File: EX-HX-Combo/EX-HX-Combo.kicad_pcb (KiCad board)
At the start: 2 copper layers, 150.2 x 124.5 mm, 41 parts, among them CN1 DB9 Male, J1 IDE_CONNECTOR, J200 Bus_Tandy_Plus_Through, J3 Bus_Tandy_Plus, SW1 SW_DIP_x10, U1 BIOS FLASH, U2 74HCT245, U3 1.8432 MHz, U4 DS1315, U5 AS6C4008-55PCN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

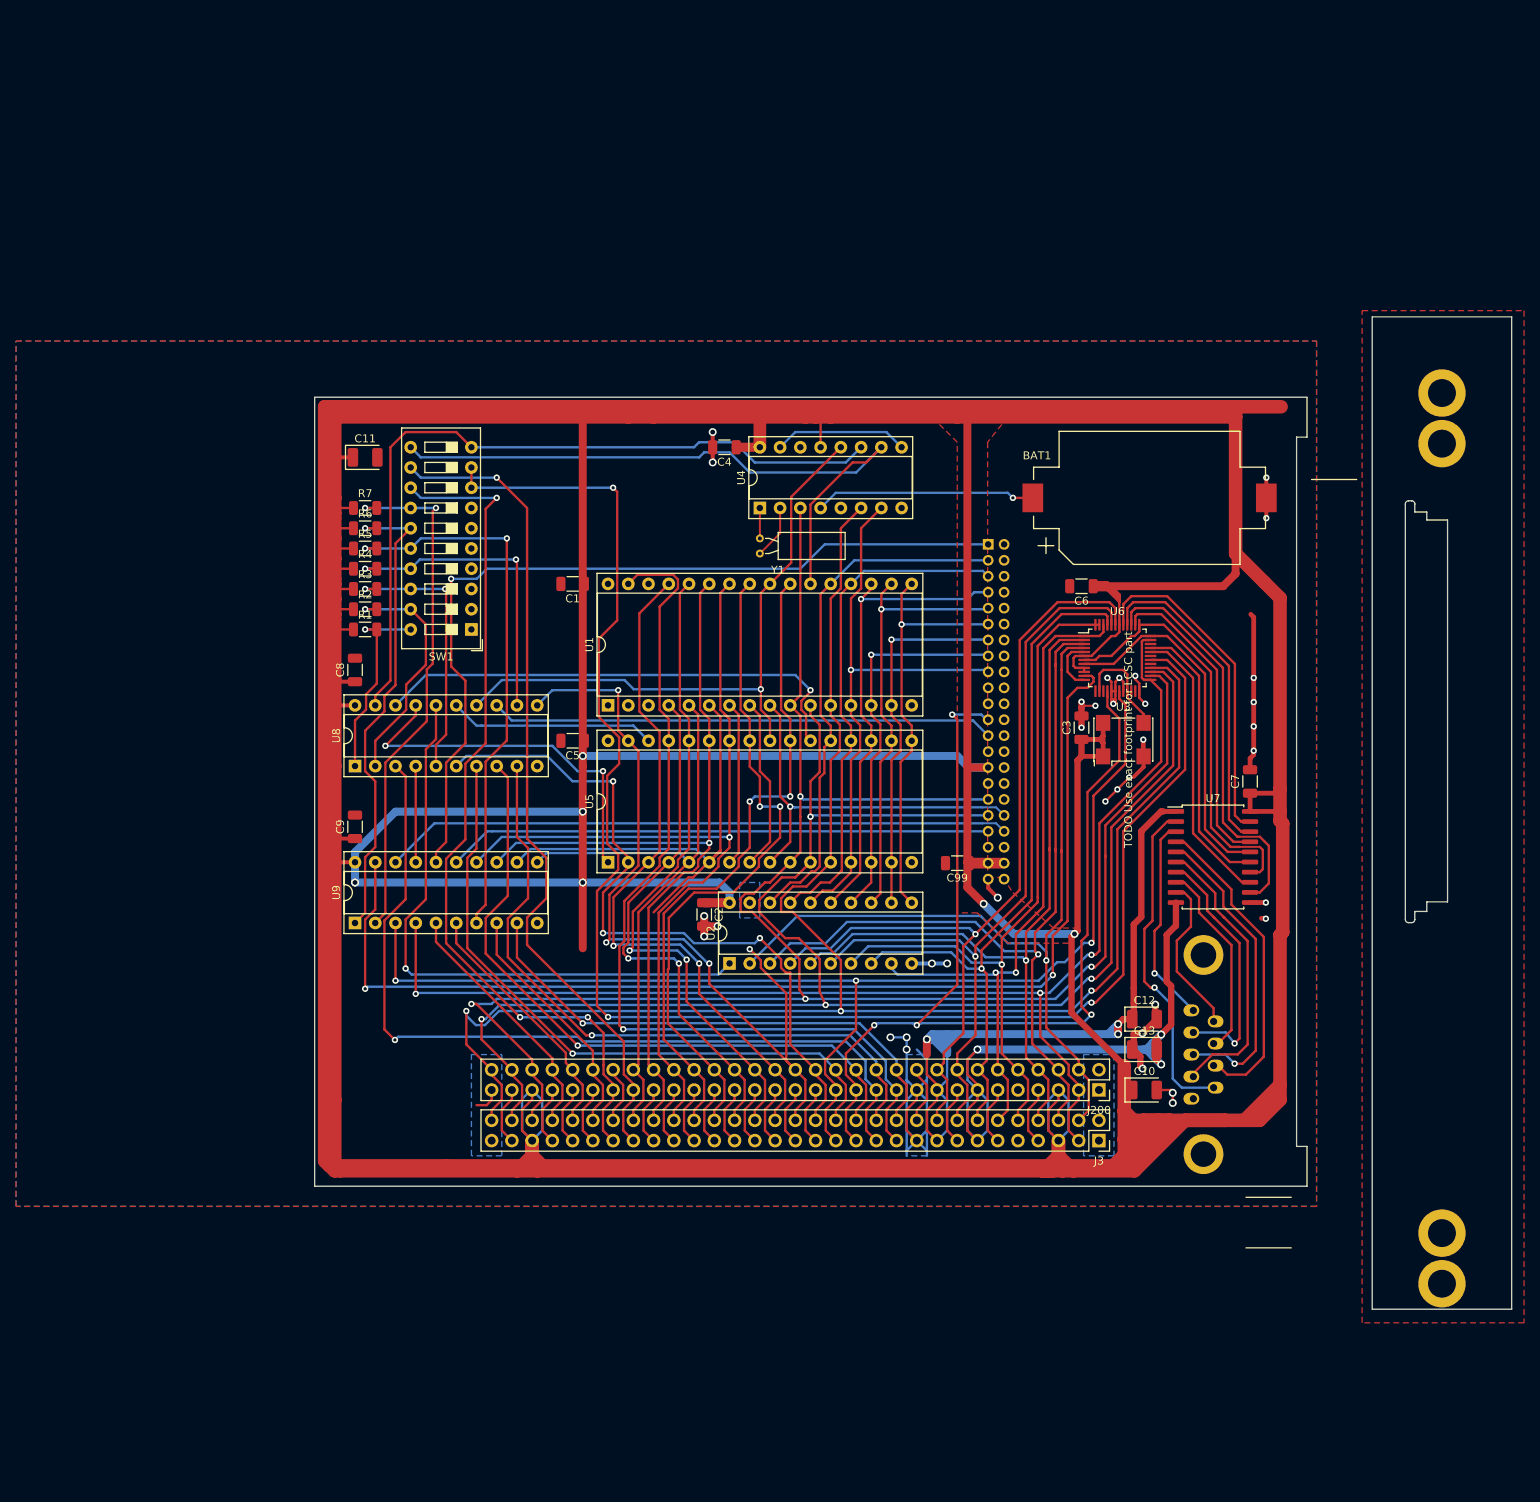
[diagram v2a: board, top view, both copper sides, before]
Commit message: EX-HX-Combo layout work: All connections have been made, in progress on tidy up.
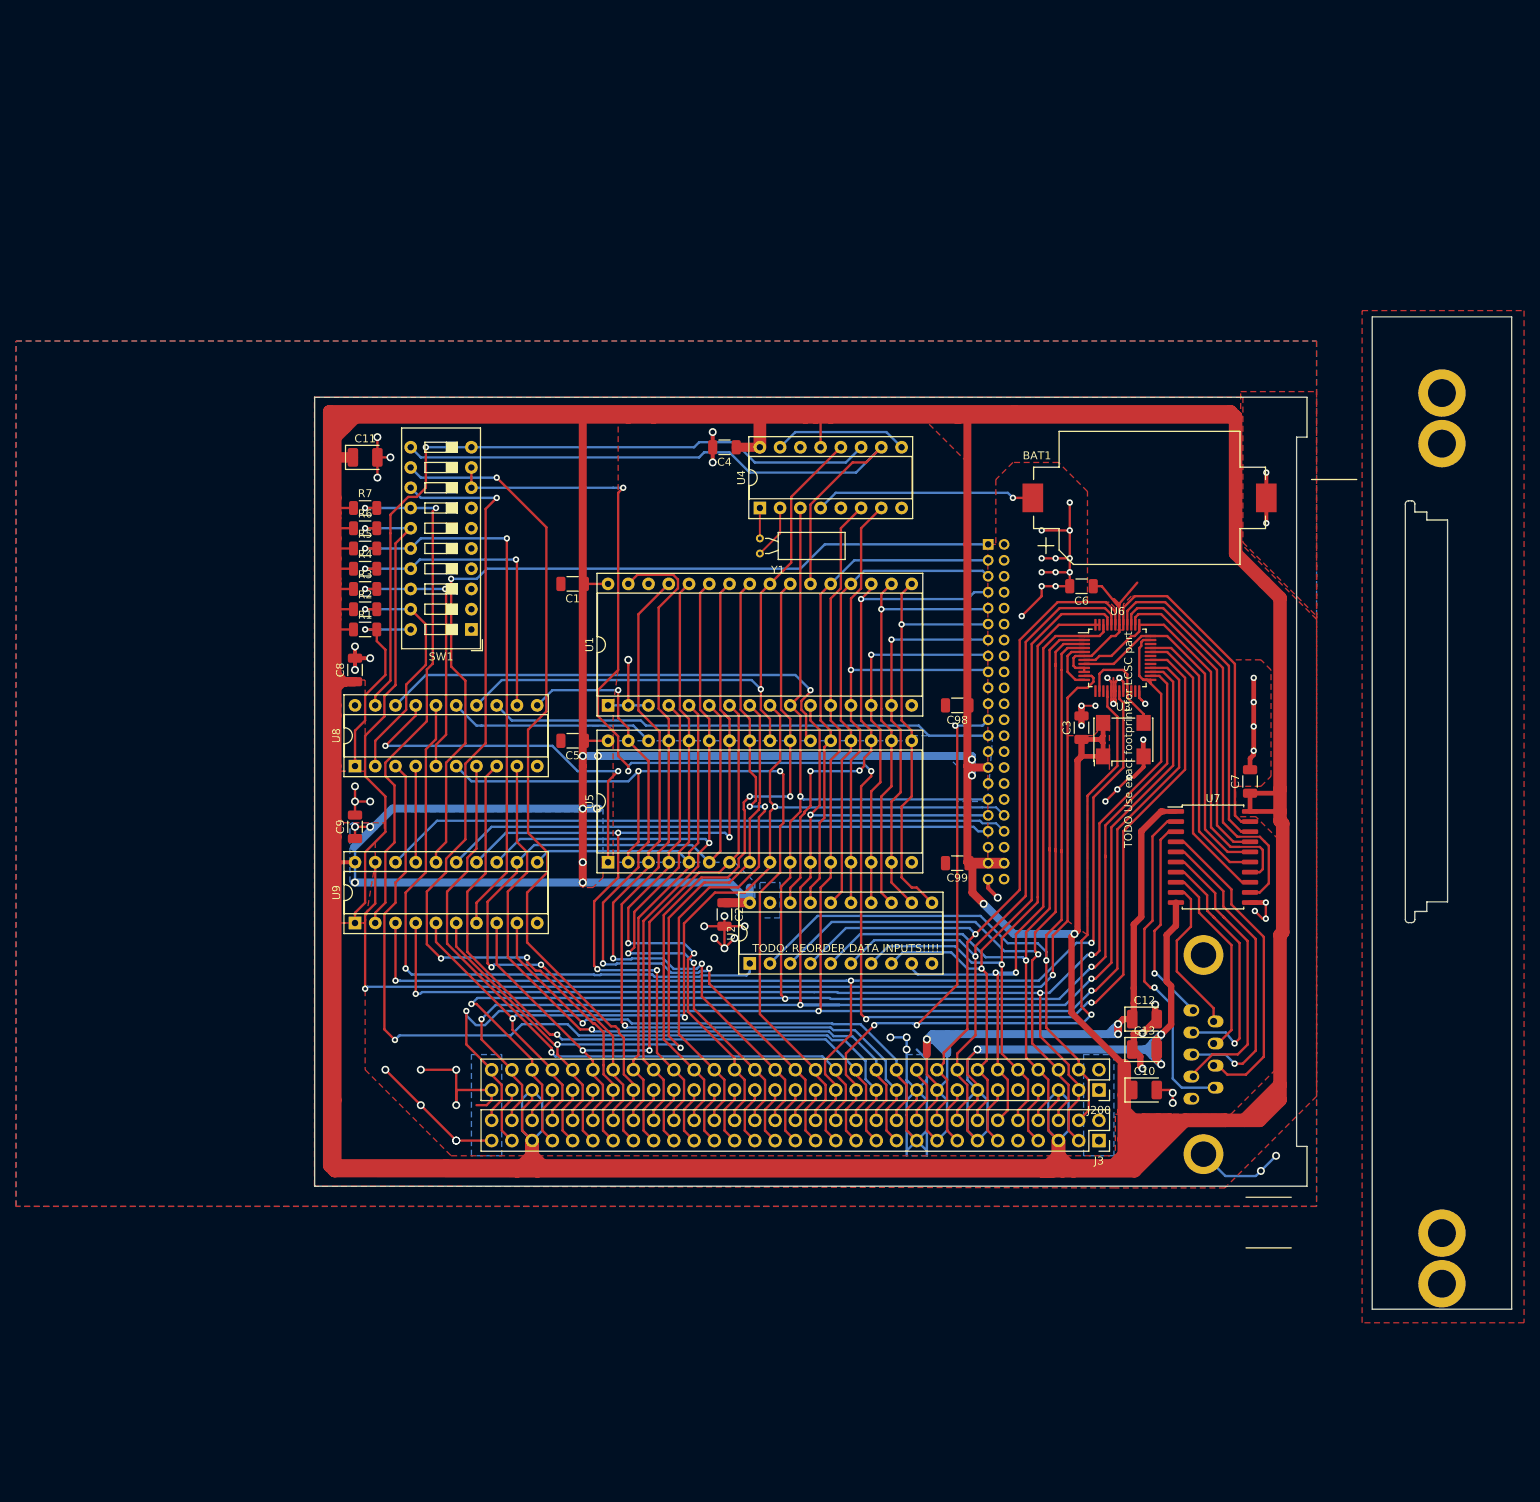
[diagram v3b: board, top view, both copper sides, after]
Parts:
- added C98: 0.1uF, Capacitor_SMD:C_1206_3216Metric, F.Cu at (200.7, 76.2)
- moved C2 2.54 mm to (171.4, 102.4)
- moved U2 2.54 mm to (174.6, 108.6)
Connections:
- U2 pad 15: D5_BUF -> D0_BUF
- U2 pad 16: D0_BUF -> D6_BUF
- U2 pad 17: D6_BUF -> D7_BUF
- U2 pad 18: D7_BUF -> D5_BUF
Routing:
- net GND: track 144.9 -> 245.8 mm, vias 36 -> 68
- net A03: track 80.9 -> 130.4 mm, vias 1 -> 3
- net A04: track 53.6 -> 98.4 mm, vias 0 -> 2
- net A05: track 51.4 -> 89.7 mm, vias 0 -> 2
- net A06: track 65.5 -> 92.4 mm, vias 0 -> 2
- net VCC: track 1310.8 -> 1286.9 mm, vias 6 -> 13
- net A15: track 102.4 -> 87.9 mm, vias 4 -> 3
- net A16: track 90.3 -> 103.0 mm, vias 3 -> 2
- net A02: track 236.2 -> 229.0 mm
- net A00: track 218.6 -> 211.7 mm
- net D5_BUF: track 59.5 -> 65.1 mm, vias 1 -> 3
- net A09: track 108.8 -> 114.0 mm, vias 1 -> 4
- net IRQ3: track 109.3 -> 113.3 mm
- net A17: track 83.3 -> 86.9 mm
- net ~CE~_BIOS_DECODE: track 95.9 -> 92.4 mm, vias 0 -> 1
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- added copper zone on B.Cu, net VCC
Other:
- board text added: "TODO: REORDER DATA INPUTS!!!!"

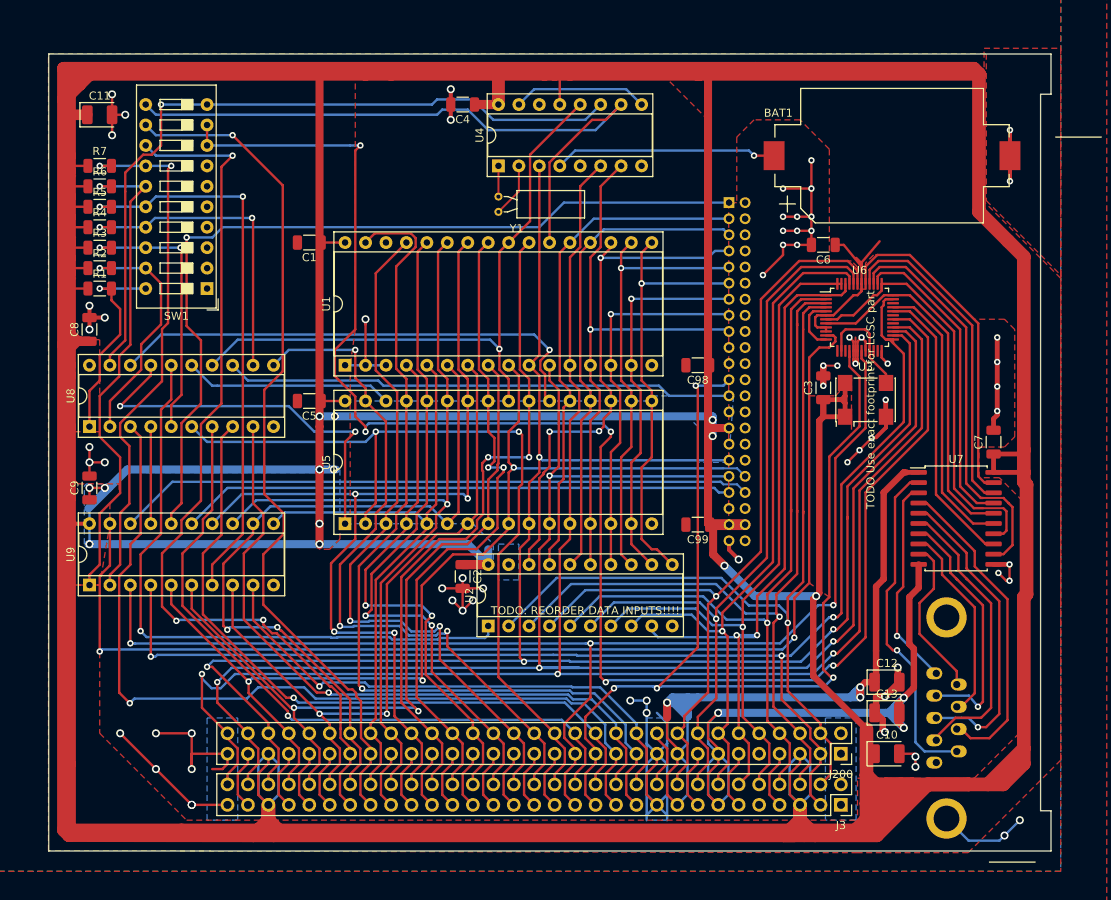
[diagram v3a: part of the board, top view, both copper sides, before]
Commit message: Add alignment tabs to EX-HX-Combo.
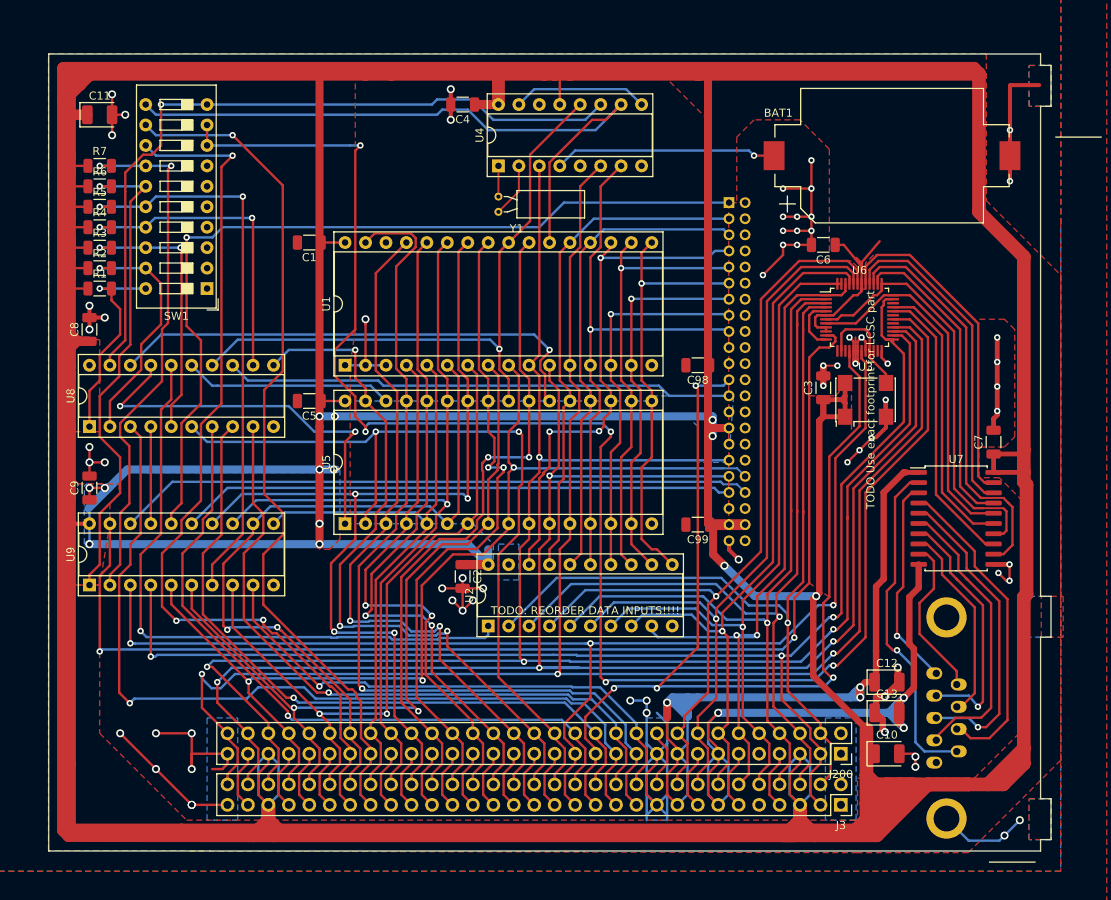
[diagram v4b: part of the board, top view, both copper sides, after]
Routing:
- net GND: track 245.8 -> 255.0 mm
- added copper zone on F.Cu, net (none)
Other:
- outline, holes or cut-outs redrawn

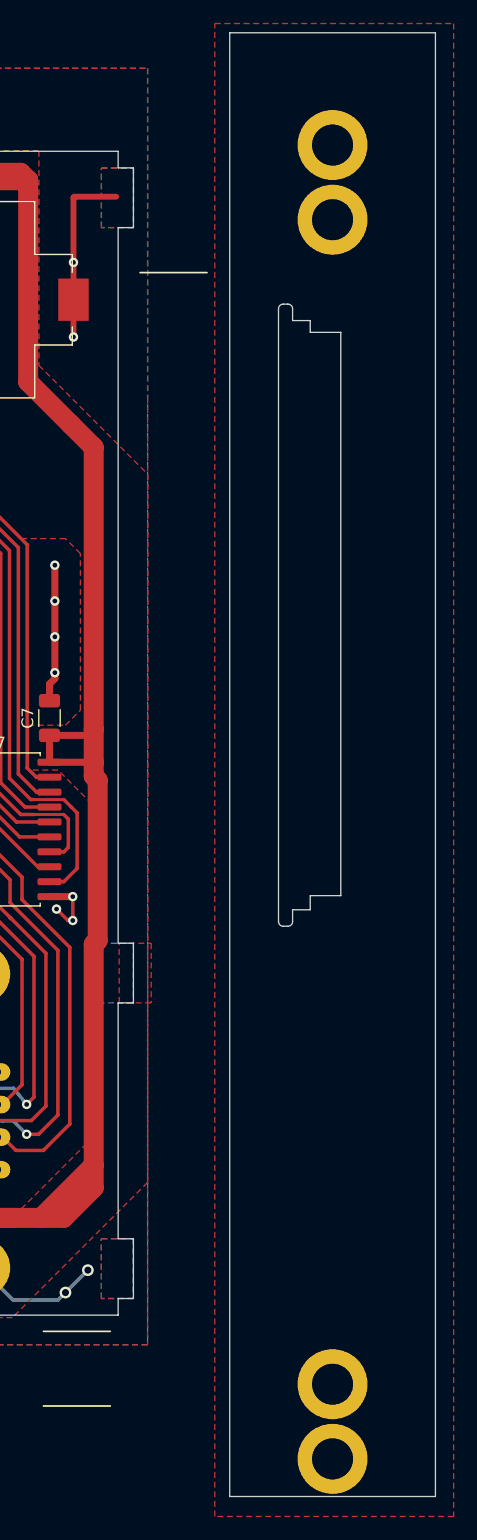
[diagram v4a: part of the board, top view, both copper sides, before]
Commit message: Add alignment holes to EX-HX-Combo.
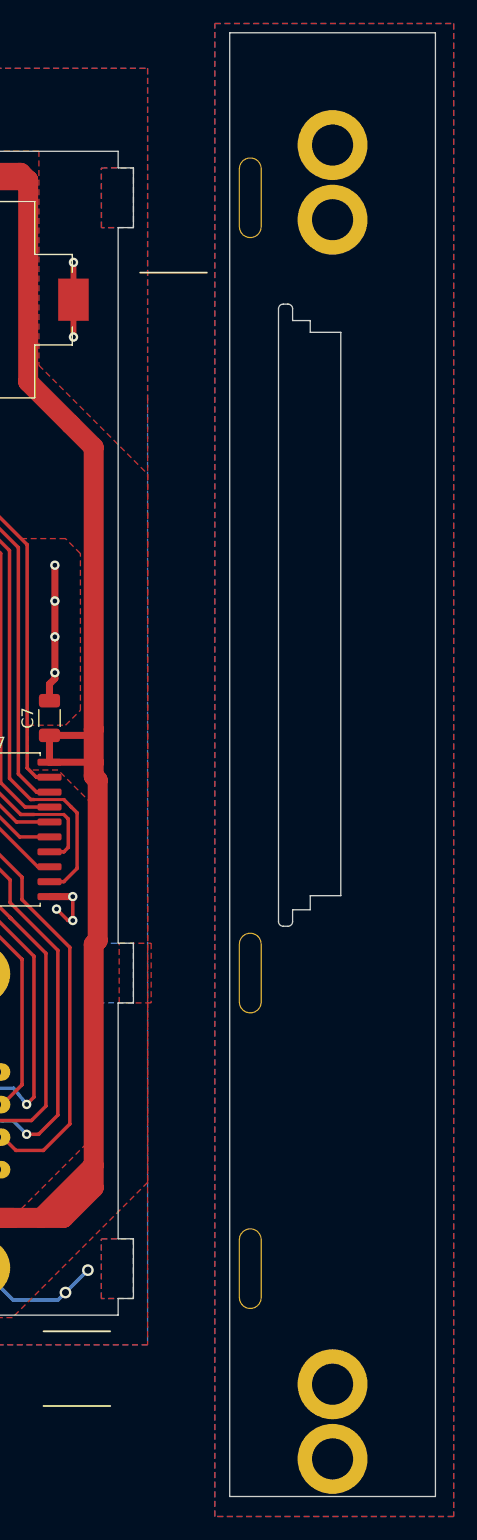
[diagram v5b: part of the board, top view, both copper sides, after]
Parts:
- added H5: AlignmentHole_Pad, 00Custom:AlignmentHole, F.Cu at (254.5, 132.6)
- added H6: AlignmentHole_Pad, 00Custom:AlignmentHole, F.Cu at (254.5, 107.4)
- added H7: AlignmentHole_Pad, 00Custom:AlignmentHole, F.Cu at (254.5, 41.5)
- renumbered H2 to H1, H3 to H2, H5 to H3, H6 to H4
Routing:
- net GND: track 255.0 -> 245.8 mm

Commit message: EX-HX-Combo layout work.
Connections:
- U2 pad 2: D7 -> D5
- U2 pad 3: D6 -> D7
- U2 pad 4: D0 -> D6
- U2 pad 5: D5 -> D0
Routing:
- net D5: track 94.4 -> 103.2 mm
- net D7: track 105.5 -> 101.4 mm
- net D6: track 102.2 -> 98.5 mm
- net D0: track 104.6 -> 101.3 mm
- net VCC: track 1286.9 -> 1288.1 mm, vias 13 -> 14
- net D4: track 90.3 -> 91.2 mm
- net ~UART_CS: track 144.8 -> 144.0 mm
- net D3: track 87.1 -> 87.8 mm
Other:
- outline, holes or cut-outs redrawn

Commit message: More EX-HX Combo layout work.
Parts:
- moved C12 1.27 mm to (224.2, 114.3)
- moved C13 0.63 mm to (224.2, 118.7)
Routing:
- net VCC: track 1288.1 -> 1307.0 mm
- net -12V: track 84.5 -> 100.4 mm
- net +12V: track 102.8 -> 96.7 mm
- net GND: track 245.8 -> 250.9 mm
